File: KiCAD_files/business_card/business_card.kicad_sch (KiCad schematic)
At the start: 81 parts, among them J1 USB_C_Receptacle_USB2.0_14P, J2 Conn_01x05_Pin, SW1 SW_MEC_5E, SW2 SW_MEC_5E, SW3 SW_MEC_5E, SW4 SW_MEC_5E, SW5 SW_MEC_5E, SW6 SW_MEC_5E, SW7 SW_MEC_5E, SW8 SW_Push, U1 STM32U073CCUx, U2 MCP1700x-300xxTT, U3 TPS3839DBZ

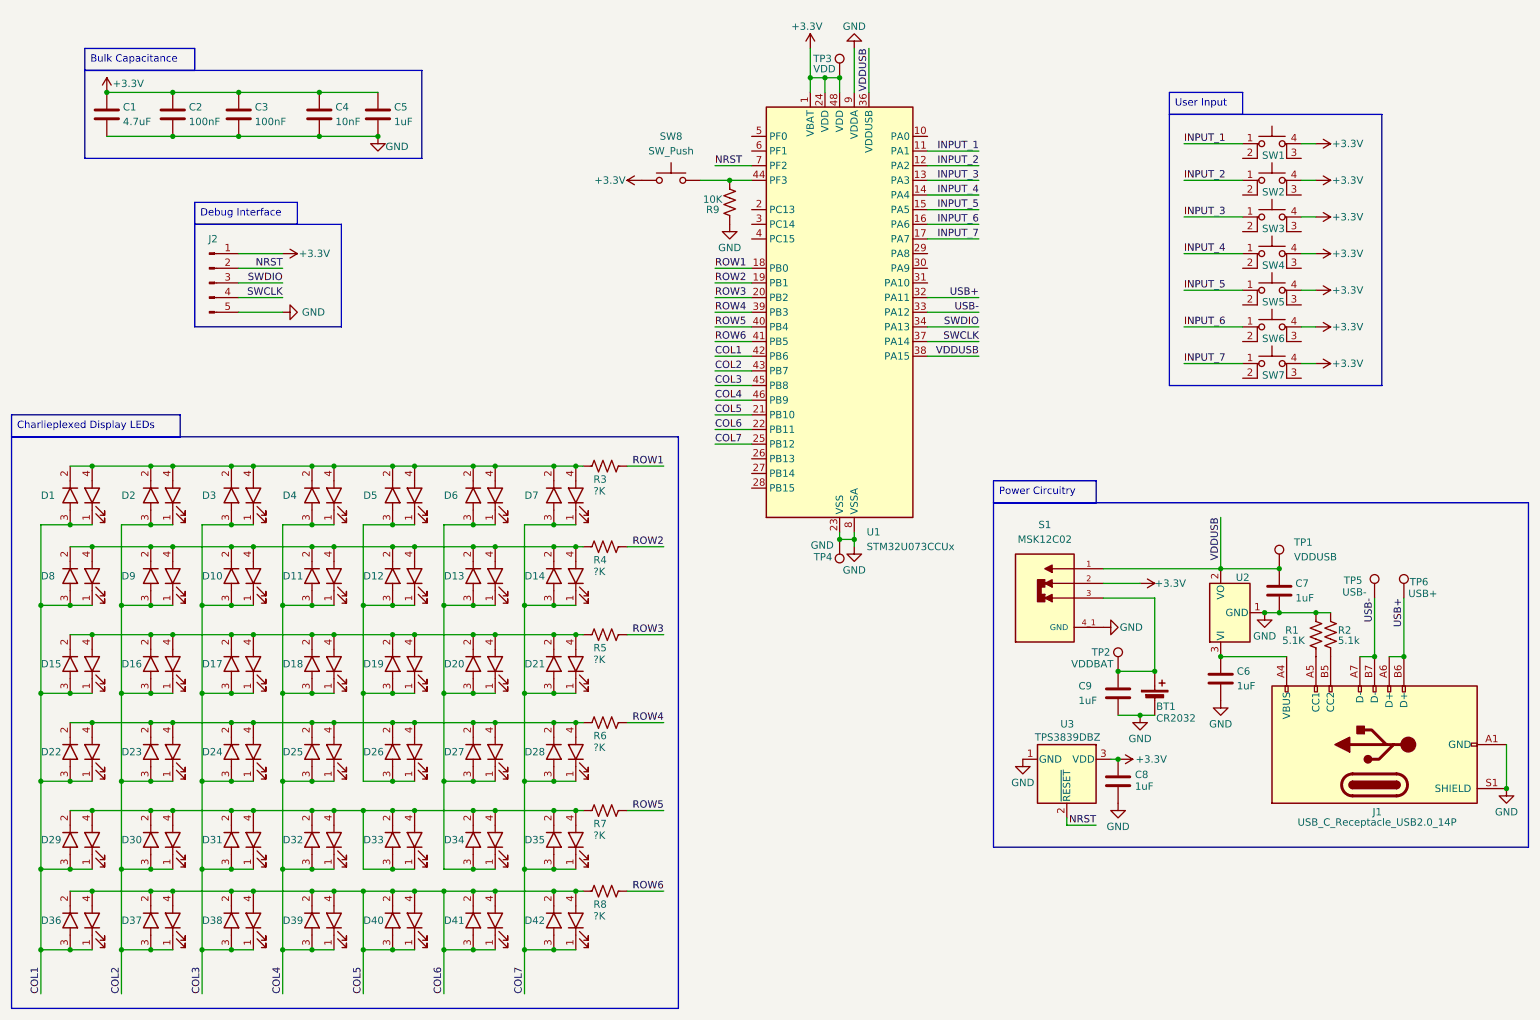
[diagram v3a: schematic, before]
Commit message: Change Connections to Match STM32C0 Spec
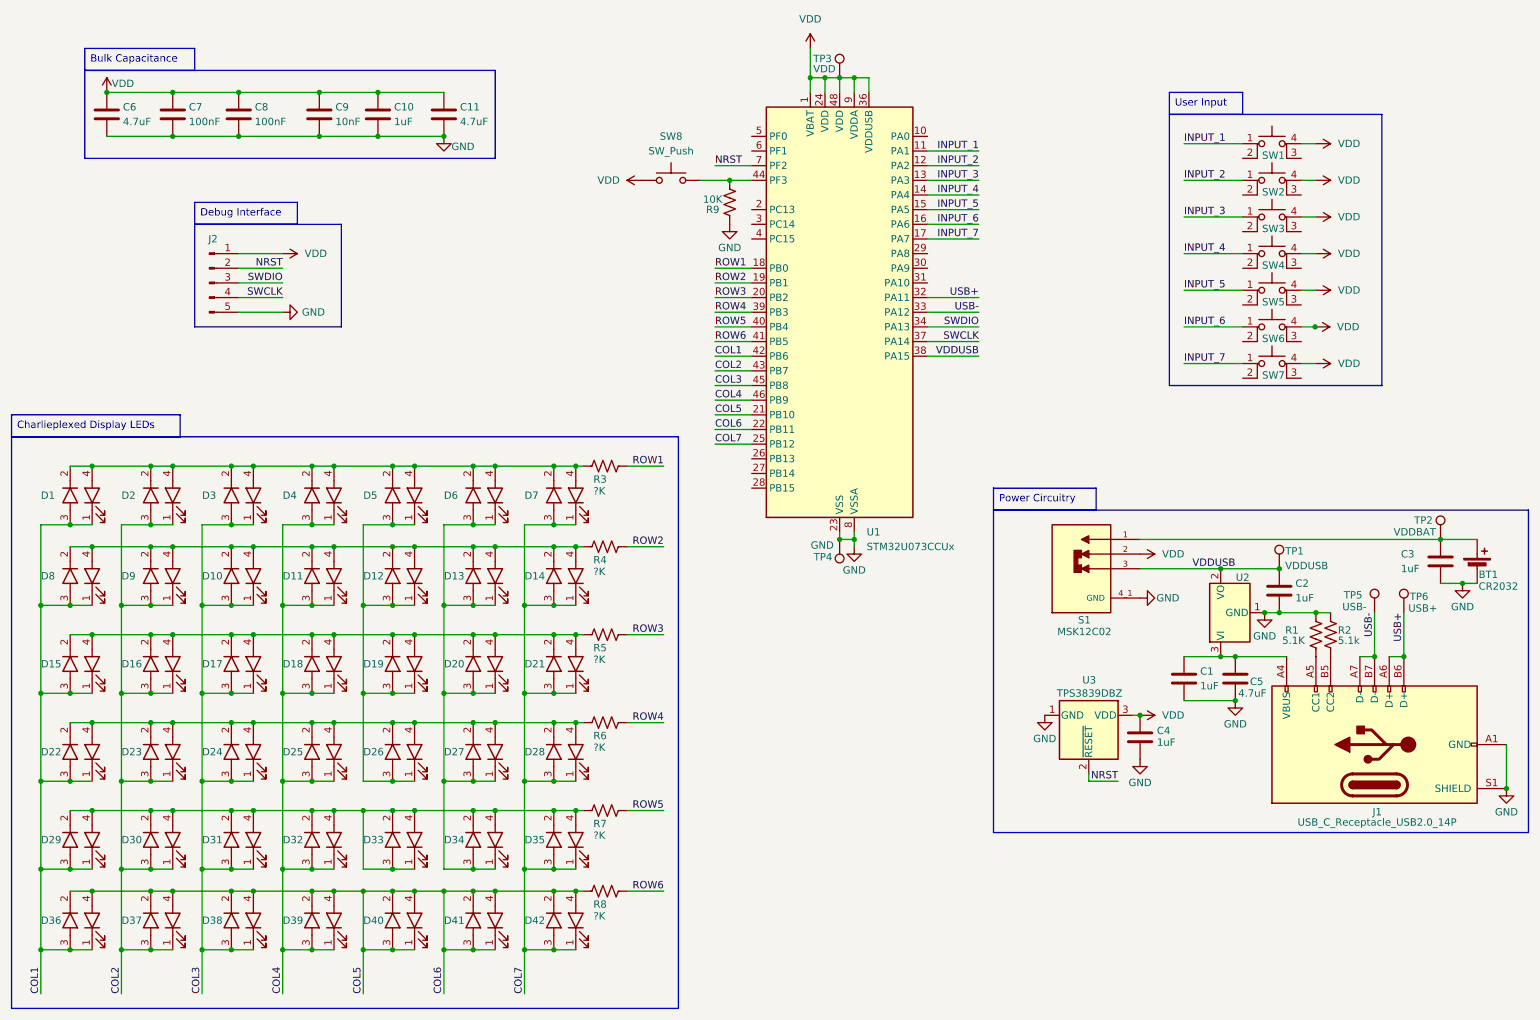
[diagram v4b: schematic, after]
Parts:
- added C11, C5: 4.7uF, Capacitor_SMD:C_0603_1608Metric, symbol Device:C
- renumbered C6 to C1, C5 to C10, C7 to C2, C9 to C3, C8 to C4, C1 to C6, C2 to C7, C3 to C8, C4 to C9
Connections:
- net GND: now also C11.2, C5.2; no longer U1.9 (VDDA)
- net VDDUSB: now also S1.3; no longer S1.1, U1.36 (VDDUSB)
- net at C1.1, J1.A4 (VBUS), J1.A9 (VBUS)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: now also C5.1
- net at BT1.1 (+), C3.1, TP2.1: now also S1.1; no longer S1.3
- net +3.3V renamed VDD
- net VDD: now also U1.36 (VDDUSB), U1.9 (VDDA), C11.1
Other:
- moved on the sheet: BT1, C1, C3, C4, S1, TP2, TP5, TP6, U3

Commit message: Move Battery Voltage Monitoring to Software
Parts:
- removed C4: 1uF, Capacitor_SMD:C_0603_1608Metric, symbol Device:C
- removed U3: TPS3839DBZ, Package_TO_SOT_SMD:SOT-23, symbol Power_Supervisor:TPS3839DBZ
- renumbered C5 to C1, C11 to C10, C1 to C2, C2 to C3, C3 to C4, C6 to C5, C7 to C6, C8 to C7, C9 to C8, C10 to C9

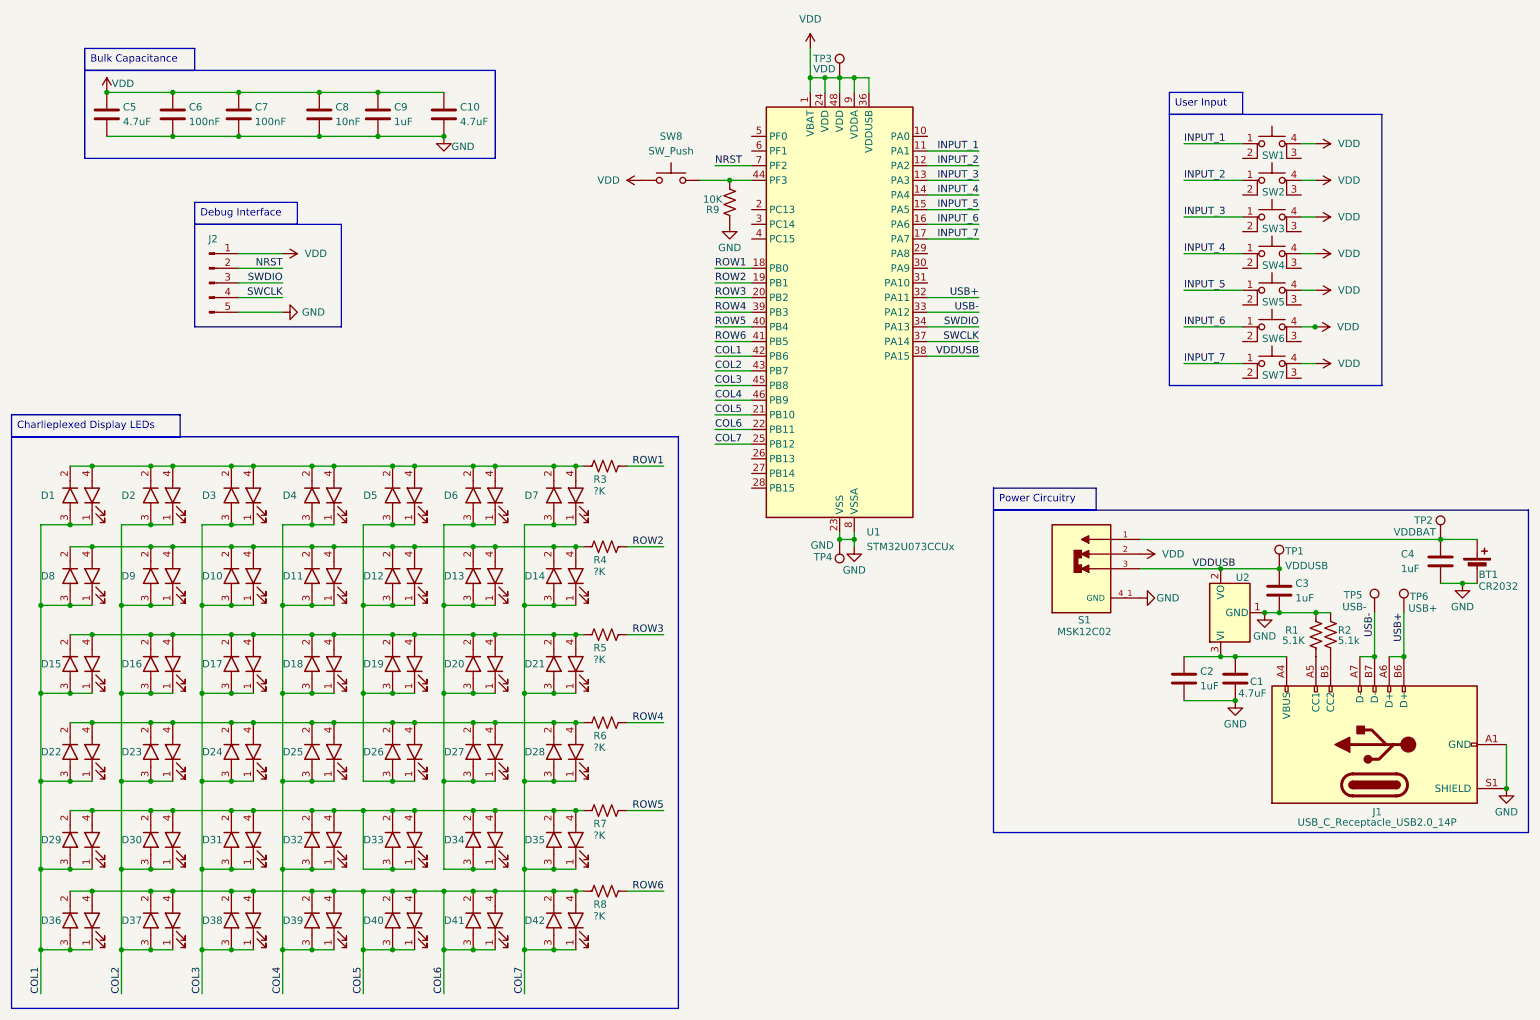
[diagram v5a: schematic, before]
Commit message: Switch Button types, Add 3D Models to Components
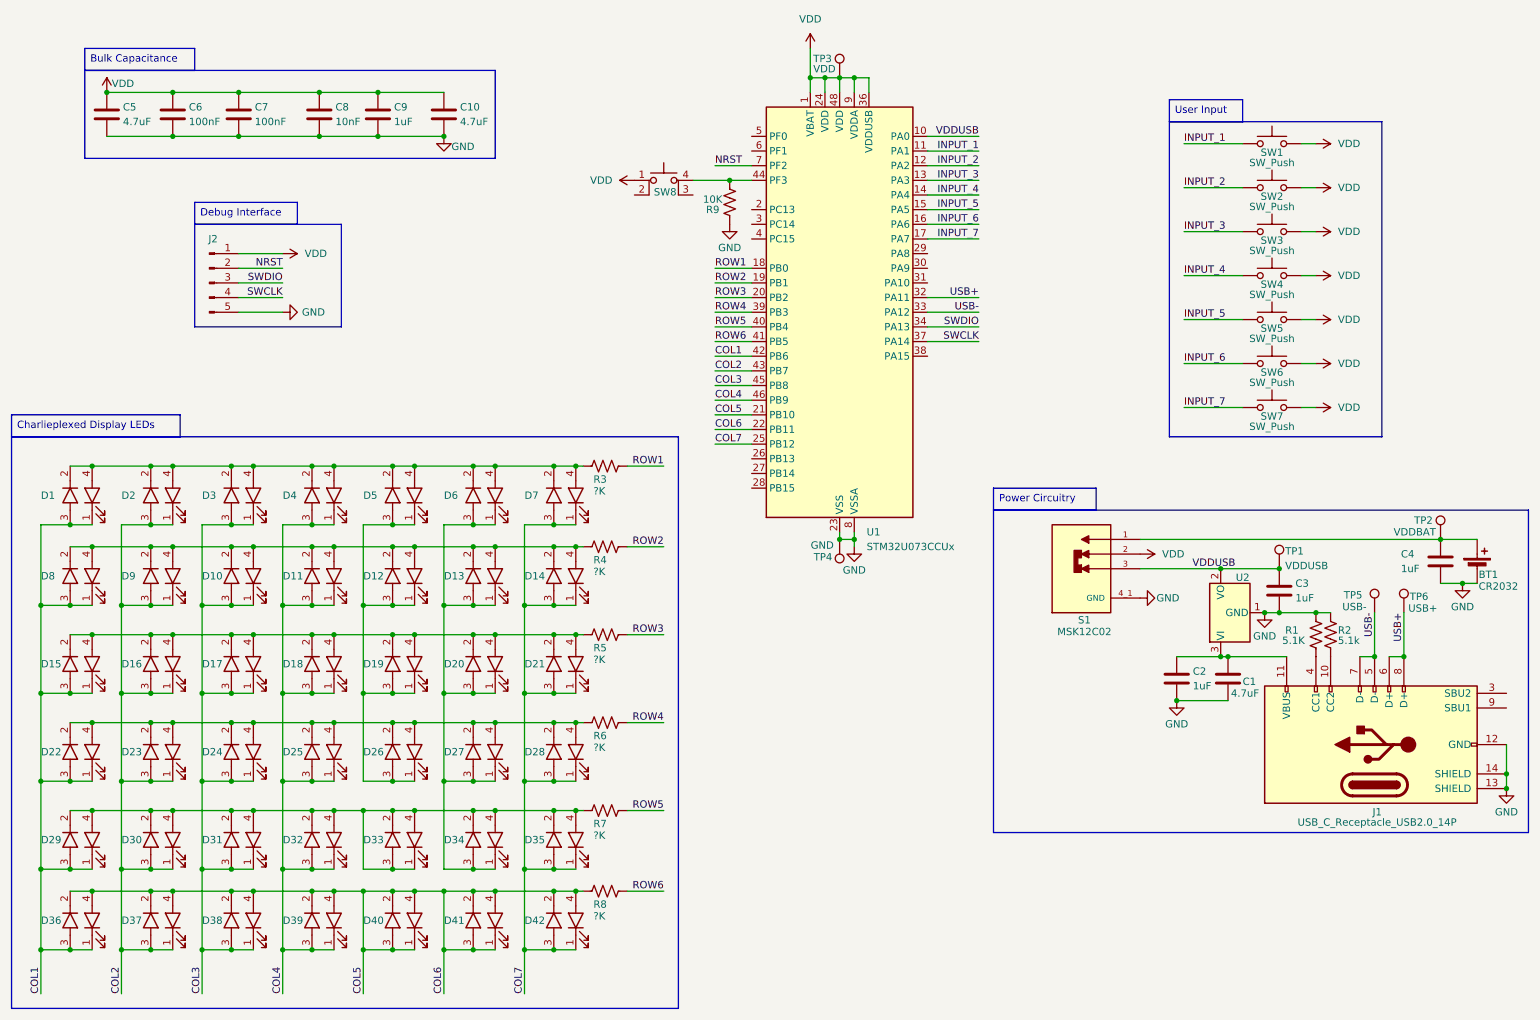
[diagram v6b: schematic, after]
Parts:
- removed SW1, SW2, SW3, SW4, SW5, SW6, SW7: SW_MEC_5E, 1TS026A-2000-0553-CT:SW-SMD_4P-L2.6-W1.6-P0.75-LS3.0, symbol Switch:SW_MEC_5E
- removed SW8: SW_Push, TSB008A2526A:TSB008A2526A, symbol Switch:SW_Push
- added SW1, SW2, SW3, SW4, SW5, SW6, SW7: SW_Push, TSB008A2526A:TSB008A2526A, symbol Switch:SW_Push
- added SW8: SW_MEC_5E, 1TS026A-2000-0553-CT:SW-SMD_4P-L2.6-W1.6-P0.75-LS3.0, symbol Switch:SW_MEC_5E
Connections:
- net GND: now also J1.1 (GND), J1.12 (GND), J1.13 (SHIELD), J1.14 (SHIELD); no longer J1.A1 (GND), J1.A12 (GND), J1.B1 (GND), J1.B12 (GND), J1.S1 (SHIELD)
- net INPUT_1: now also SW1.1
- net INPUT_2: now also SW2.1
- net INPUT_3: now also SW3.1
- net INPUT_4: now also SW4.1
- net INPUT_5: now also SW5.1
- net INPUT_6: now also SW6.1
- net INPUT_7: now also SW7.1
- net USB+: now also J1.6 (D+), J1.8 (D+); no longer J1.A6 (D+), J1.B6 (D+)
- net USB-: now also J1.5 (D-), J1.7 (D-); no longer J1.A7 (D-), J1.B7 (D-)
- net VDD: now also SW1.2, SW2.2, SW3.2, SW4.2, SW5.2, SW6.2, SW7.2, SW8.1
- net VDDUSB: now also U1.10 (PA0); no longer U1.38 (PA15)
- net at R9.1, U1.44 (PF3): now also SW8.4 (A)
- net at R1.2: now also J1.4 (CC1); no longer J1.A5 (CC1)
- net at R2.2: now also J1.10 (CC2); no longer J1.B5 (CC2)
- new net: C1.1, C2.1, J1.11 (VBUS), J1.2 (VBUS), U2.3 (VI)
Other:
- moved on the sheet: C1, C2

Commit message: PCB Layout
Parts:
- removed TP4: GND, TestPoint:TestPoint_THTPad_D1.0mm_Drill0.5mm, symbol Connector:TestPoint
- removed TP5: USB-, TestPoint:TestPoint_THTPad_D1.0mm_Drill0.5mm, symbol Connector:TestPoint
- removed TP6: USB+, TestPoint:TestPoint_THTPad_D1.0mm_Drill0.5mm, symbol Connector:TestPoint
- added C11: 100nF, Capacitor_SMD:C_0603_1608Metric, symbol Device:C
- TP2: value VDDBAT -> GND
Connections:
- net COL5: now also D12.1, D12.3, D19.1, D19.3, D26.1, D26.3, D33.1, D33.3, D5.1, D5.3; no longer D36.2, D36.4, D37.2, D37.4, D38.2, D38.4, D39.2, D39.4, D40.2, D40.4, D41.1, D41.2, D41.3, D41.4, D42.2, D42.4, R8.1, U1.22 (PB11)
- net GND: now also TP2.1, C11.2
- net VDD: now also C11.1
- net VDDUSB: now also S1.1; no longer S1.3
- net COL6: now reaches D13.1, D13.3, D20.1, D20.3, D27.1, D27.3, D34.1, D34.3, D6.1, D6.3
- net COL6: now also D41.1, D41.3, U1.22 (PB11)
- net at D29.2, D29.4, D30.2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: no longer D33.1, D33.3
- net at BT1.1 (+), C4.1: now also S1.3; no longer S1.1, TP2.1
- new net: D36.2, D36.4, D37.2, D37.4, D38.2, D38.4, D39.2, D39.4, D40.2, D40.4, D41.2, D41.4, D42.2, D42.4, R8.1
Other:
- moved on the sheet: BT1, C10, C4, C5, C6, C7, C8, C9, S1

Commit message: Finish Initial PCB Layout
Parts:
- added R10: 10K, Resistor_SMD:R_0603_1608Metric, symbol Device:R_US
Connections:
- net NRST: now also J2.3 (Pin_3); no longer J2.2 (Pin_2)
- net ROW1: now also U1.41 (PB5); no longer U1.18 (PB0)
- net ROW2: now also U1.40 (PB4); no longer U1.19 (PB1)
- net ROW3: now also U1.39 (PB3); no longer U1.20 (PB2)
- net ROW4: now also U1.20 (PB2); no longer U1.39 (PB3)
- net ROW5: now also U1.19 (PB1); no longer U1.40 (PB4)
- net ROW6: now also U1.18 (PB0); no longer U1.41 (PB5)
- net SWDIO: now also J2.2 (Pin_2); no longer J2.3 (Pin_3)
- net VDD: now also SW8.2
- net VDDUSB: now also R10.1; no longer U1.10 (PA0)
- net at U1.29 (PA8): now also R10.2
- net at R9.1, SW8.4 (A), U1.44 (PF3): now also SW8.3 (K)
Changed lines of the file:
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@@
 	)
 	(junction
+		(at 125.73 46.99)
+		(diameter 0)
+		(color 0 0 0 0)
+	)
+	(junction
 		(at 69.85 110.49)
 		(diameter 0)
@@
 	)
 	(junction
+		(at 135.89 46.99)
+		(diameter 0)
+		(color 0 0 0 0)
+	)
+	(junction
 		(at 31.75 140.97)
 		(diameter 0)
@@
 	(wire
 		(pts
-			(xy 185.42 39.37) (xy 176.53 39.37)
-		)
-		(stroke
-			(width 0)
-			(type default)
-		)
-	)
-	(wire
-		(pts
 			(xy 41.91 170.18) (xy 45.72 170.18)
 		)
@@
 	(wire
 		(pts
+			(xy 125.73 46.99) (xy 125.73 49.53)
+		)
+		(stroke
+			(width 0)
+			(type default)
+		)
+	)
+	(wire
+		(pts
 			(xy 101.6 110.49) (xy 111.76 110.49)
 		)
@@
 	(wire
 		(pts
+			(xy 135.89 46.99) (xy 135.89 49.53)
+		)
+		(stroke
+			(width 0)
+			(type default)
+		)
+	)
+	(wire
+		(pts
 			(xy 45.72 96.52) (xy 55.88 96.52)
 		)
@@
 	(wire
 		(pts
+			(xy 176.53 59.69) (xy 184.15 59.69)
+		)
+		(stroke
+			(width 0)
+			(type default)
+		)
+	)
+	(wire
+		(pts
 			(xy 220.98 48.26) (xy 231.14 48.26)
 		)
@@
 	(wire
 		(pts
+			(xy 200.66 59.69) (xy 191.77 59.69)
+		)
+		(stroke
+			(width 0)
+			(type default)
+		)
+	)
+	(wire
+		(pts
 			(xy 36.83 151.13) (xy 41.91 151.13)
 		)
@@
 		)
 	)
-	(label "ROW6"
-		(at 139.7 74.93 0)
-		(effects
-			(font
-				(size 1.27 1.27)
-			)
-			(justify left bottom)
-		)
-	)
-	(label "ROW2"
-		(at 139.7 64.77 0)
+	(label "VDDUSB"
+		(at 200.66 59.69 180)
 		(effects
 			(font
 				(size 1.27 1.27)
 			)
-			(justify left bottom)
+			(justify right bottom)
 		)
 	)
@@
 		)
 	)
-	(label "SWDIO"
-		(at 64.77 64.77 180)
-		(effects
-			(font
-				(size 1.27 1.27)
-			)
-			(justify right bottom)
-		)
-	)
 	(label "INPUT_4"
 		(at 220.98 63.5 0)
@@
 		)
 	)
+	(label "ROW4"
+		(at 139.7 67.31 0)
+		(effects
+			(font
+				(size 1.27 1.27)
+			)
+			(justify left bottom)
+		)
+	)
 	(label "SWCLK"
 		(at 64.77 67.31 180)
@@
 		)
 	)
-	(label "ROW5"
-		(at 139.7 72.39 0)
+	(label "ROW1"
+		(at 139.7 74.93 0)
 		(effects
 			(font
@@
 		)
 	)
+	(label "SWDIO"
+		(at 64.77 62.23 180)
+		(effects
+			(font
+				(size 1.27 1.27)
+			)
+			(justify right bottom)
+		)
+	)
 	(label "INPUT_6"
 		(at 185.42 54.61 180)
@@
 	)
 	(label "ROW3"
+		(at 139.7 69.85 0)
+		(effects
+			(font
+				(size 1.27 1.27)
+			)
+			(justify left bottom)
+		)
+	)
+	(label "ROW3"
 		(at 130.81 125.73 180)
 		(effects
@@
 		)
 	)
+	(label "NRST"
+		(at 64.77 64.77 180)
+		(effects
+			(font
+				(size 1.27 1.27)
+			)
+			(justify right bottom)
+		)
+	)
 	(label "ROW4"
 		(at 130.81 140.97 180)
@@
 		)
 	)
-	(label "NRST"
-		(at 64.77 62.23 180)
-		(effects
-			(font
-				(size 1.27 1.27)
-			)
-			(justify right bottom)
-		)
-	)
 	(label "COL3"
 		(at 50.8 187.96 90)
@@
 		)
 	)
-	(label "COL5"
-		(at 78.74 187.96 90)
+	(label "ROW2"
+		(at 139.7 72.39 0)
 		(effects
 			(font
@@
 		)
 	)
-	(label "ROW4"
-		(at 139.7 69.85 0)
+	(label "COL5"
+		(at 78.74 187.96 90)
 		(effects
 			(font
@@
 		)
 	)
-	(label "ROW3"
-		(at 139.7 67.31 0)
-		(effects
-			(font
-				(size 1.27 1.27)
-			)
-			(justify left bottom)
-		)
-	)
 	(label "SWCLK"
 		(at 185.42 74.93 180)
@@
 		)
 	)
-	(label "ROW1"
+	(label "ROW6"
 		(at 139.7 62.23 0)
 		(effects
@@
 		)
 	)
-	(label "VDDUSB"
-		(at 185.42 39.37 180)
+	(label "ROW5"
+		(at 139.7 64.77 0)
 		(effects
 			(font
 				(size 1.27 1.27)
 			)
-			(justify right bottom)
+			(justify left bottom)
 		)
 	)
@@
 					(unit 1)
 				)
+			)
+		)
+	)
+	(symbol
+		(lib_id "Device:R_US")
+		(at 187.96 59.69 270)
+		(unit 1)
+		(exclude_from_sim no)
+		(in_bom yes)
+		(on_board yes)
+		(dnp no)
+		(property "Reference" "R10"
+			(at 189.738 63.754 90)
+			(effects
+				(font
+					(size 1.27 1.27)
+				)
+				(justify right)
+			)
+		)
+		(property "Value" "10K"
+			(at 189.738 61.976 90)
+			(effects
+				(font
+					(size 1.27 1.27)
+				)
+				(justify right)
+			)
+		)
+		(property "Footprint" "Resistor_SMD:R_0603_1608Metric"
+			(at 187.706 60.706 90)
+			(effects
+				(font
+					(size 1.27 1.27)
+				)
+				(hide yes)
+			)
+		)
+		(property "Datasheet" "~"
+			(at 187.96 59.69 0)
+			(effects
+				(font
+					(size 1.27 1.27)
+				)
+				(hide yes)
+			)
+		)
+		(property "Description" "Resistor, US symbol"
+			(at 187.96 59.69 0)
+			(effects
+				(font
+					(size 1.27 1.27)
+				)
+				(hide yes)
+			)
+		)
+		(pin "1"
+		)
+		(pin "2"
+		)
+		(instances
+			(project "business_card"
+				(path "/16d1a3fe-4f2d-4eb3-9740-21c0af2e4feb"
+					(reference "R10")
+					(unit 1)
+				)
